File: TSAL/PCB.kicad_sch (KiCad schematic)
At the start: 62 parts, among them J1 TE 770966-2, J2 JST B04B-XASK, J3 Conn_01x02, J4 Conn_01x02, Q1 IRLZ44N, Q2 MMBT3904, Q3 IRLZ44N, U1 TL431D, U2 LMV331, U3 UCC12040DVE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

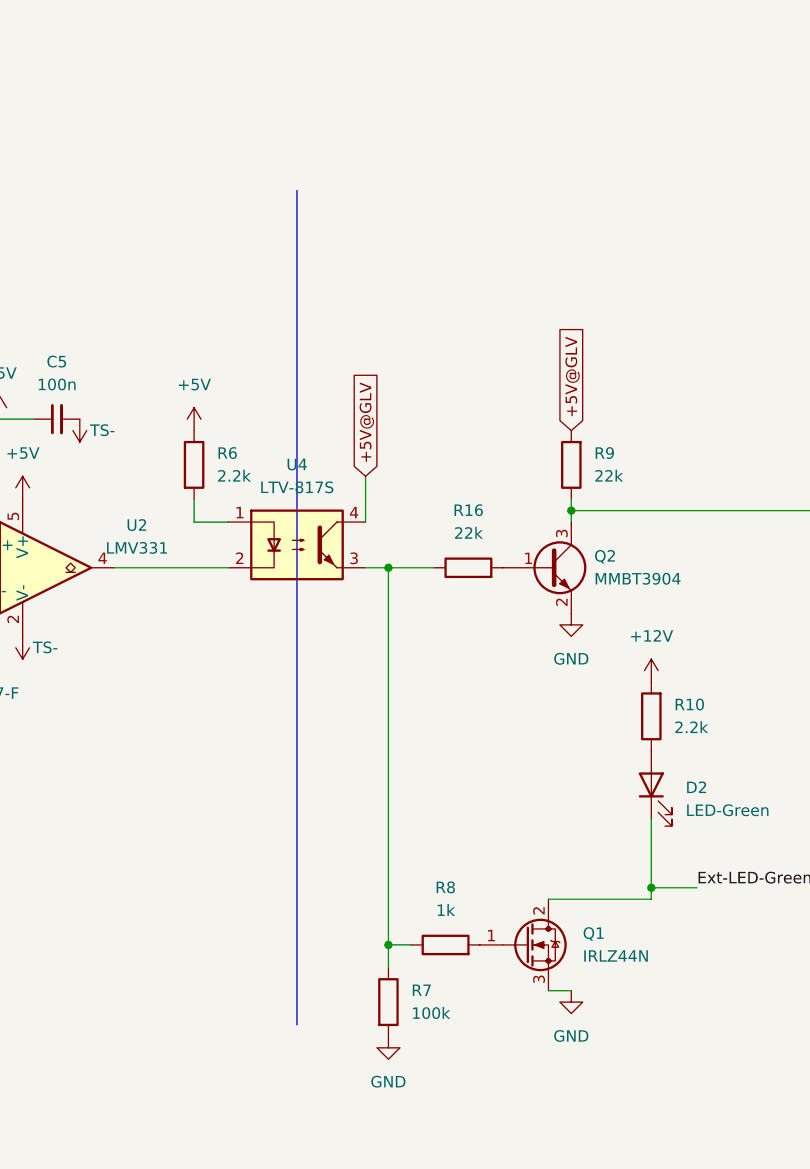
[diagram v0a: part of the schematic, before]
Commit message: fix low voltage circuit
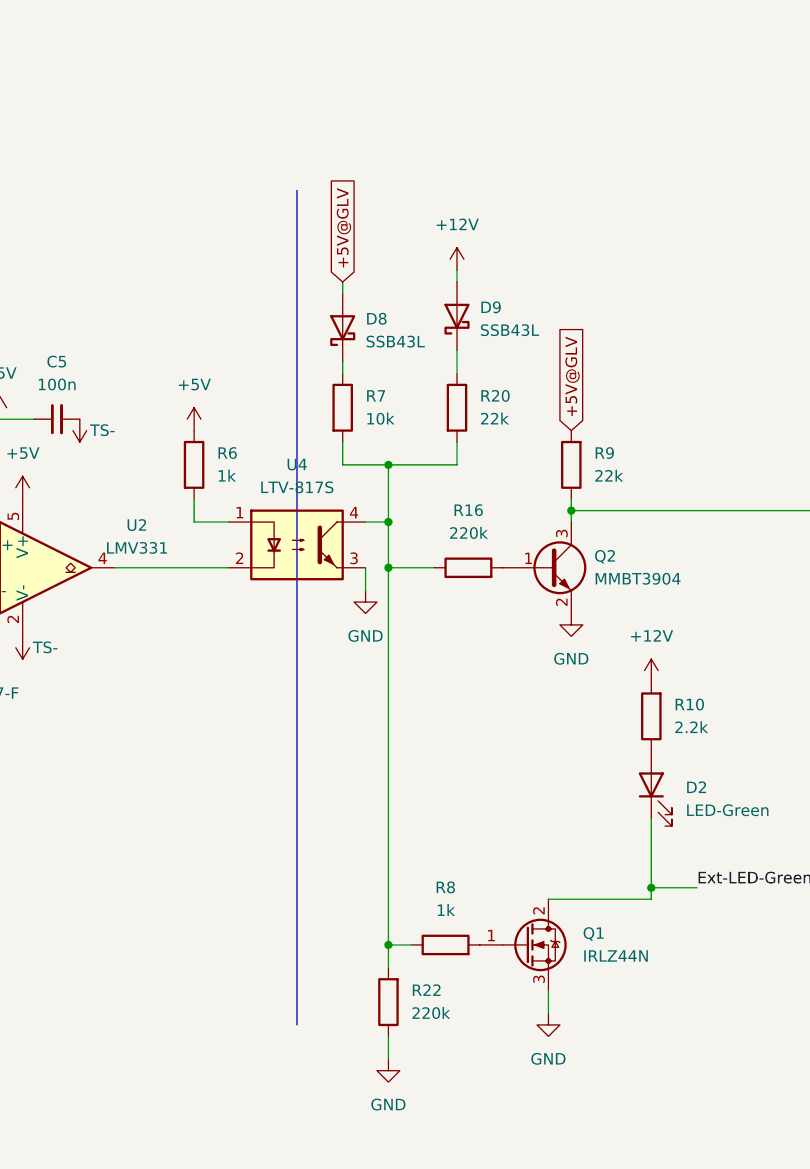
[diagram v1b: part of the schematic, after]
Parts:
- added D8, D9: SSB43L, Diode_SMD:D_SMB, symbol Device:D_Schottky
- added R20: 22k, Resistor_SMD:R_0603_1608Metric, symbol Device:R
- added R22: 220k, Resistor_SMD:R_0603_1608Metric, symbol Device:R
- R16: value 22k -> 220k
- R6: value 2.2k -> 1k
- R7: value 100k -> 10k
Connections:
- net +12V: now also D9.2 (A)
- net +5V@GLV: now also D8.2 (A); no longer U4.4
- net GND: now also U4.3, R22.1; no longer R7.2
- net at R16.1, R8.1: now also R7.2, U4.4, R20.2, R22.2; no longer R7.1, U4.3
- new net: D8.1 (K), R7.1
- new net: D9.1 (K), R20.1

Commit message: TSAL REV3 :(
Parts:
- removed D4: AES2JF-HF, KiCADv6:CR_SMAF_CIP, symbol Device:D_Schottky
- added C15: 100u, Capacitor_SMD:CP_Elec_6.3x7.7, symbol Device:C_Polarized_Small
- added C8: 470p, Capacitor_SMD:C_0603_1608Metric, symbol Device:C_Small
- added D10: 1N4148WS, Diode_SMD:D_SOD-123, symbol Device:D
- added D4: STTH1R06A, Diode_SMD:D_SMA, symbol Device:D
- added JP1: SolderJumper_2_Bridged, Jumper:SolderJumper-2_P1.3mm_Bridged_RoundedPad1.0x1.5mm, symbol Jumper:SolderJumper_2_Bridged
- added R23: 24k, Resistor_SMD:R_0603_1608Metric, symbol Device:R_Small
- added R24: 1k, Resistor_SMD:R_0603_1608Metric, symbol Device:R_Small
- added TP1, TP2, TP3, TP4, TP5, TP6: TestPoint, TestPoint:TestPoint_Keystone_5019_Minature, symbol Connector:TestPoint
- added U6: LF50_TO252, Package_TO_SOT_SMD:TO-252-2, symbol Regulator_Linear:LF50_TO252
- C1: value 100n -> 220n
- C2: value 100u -> 0.1u; now not fitted
- L1: footprint Inductor_SMD:L_1008_2520Metric -> Inductor_SMD:L_12x12mm_H8mm
- R17, R18: value 5k -> 20k
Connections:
- net +5V: now also JP1.2 (B), R24.1, U6.3 (VO); no longer C2.1, D6.2 (A), L1.2
- net TS-: now also C15.2, D4.2 (A), R24.2, TP6.1, U6.2 (GND)
- net at C1.1, D6.1 (K), R17.1: now also D10.2 (A)
- net at R17.2, R18.1, U7.2 (FB): now also C8.1, TP2.1
- net at RV1.2, U2.1 (+): now also TP5.1
- net at C1.2, C7.2, L1.1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: now also C8.2, D4.1 (K), TP3.1
- net at C7.1, U7.1 (VCC): now also R23.1, TP1.1
- new net: C15.1, C2.1, D6.2 (A), JP1.1 (A), L1.2, TP4.1, U6.1 (VI)
- new net: D10.1 (K), R23.2
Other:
- moved on the sheet: C1, C10, C11, C12, C13, C14, C3, C4, C5, C6, C7, C9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

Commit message: TSAL V3 Minor changes
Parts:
- H1, H2, H3, H4: footprint MountingHole:MountingHole_4mm -> MountingHole:MountingHole_3.2mm_M3
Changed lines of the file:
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@@
   (symbol (lib_id "Mechanical:MountingHole") (at 88.9 233.68 0) (unit 1)
     (in_bom yes) (on_board yes) (dnp no)
-    (property "Reference" "H3" (at 88.9 228.6 0)
-      (effects (font (size 1.27 1.27)))
-    )
-    (property "Value" "MountingHole" (at 88.9 230.505 0)
-      (effects (font (size 1.27 1.27)))
-    )
-    (property "Footprint" "MountingHole:MountingHole_4mm" (at 88.9 233.68 0)
+    (property "Reference" "H3" (at 92.71 232.41 0)
+      (effects (font (size 1.27 1.27)))
+    )
+    (property "Value" "MountingHole" (at 97.79 234.95 0)
+      (effects (font (size 1.27 1.27)))
+    )
+    (property "Footprint" "MountingHole:MountingHole_3.2mm_M3" (at 88.9 233.68 0)
       (effects (font (size 1.27 1.27)) hide)
     )
@@
       (effects (font (size 1.27 1.27)) (justify left))
     )
-    (property "Footprint" "MountingHole:MountingHole_4mm" (at 88.9 240.03 0)
+    (property "Footprint" "MountingHole:MountingHole_3.2mm_M3" (at 88.9 240.03 0)
       (effects (font (size 1.27 1.27)) hide)
     )
@@
   (symbol (lib_id "Mechanical:MountingHole") (at 88.9 224.79 0) (unit 1)
     (in_bom yes) (on_board yes) (dnp no)
-    (property "Reference" "H2" (at 88.9 219.71 0)
-      (effects (font (size 1.27 1.27)))
-    )
-    (property "Value" "MountingHole" (at 88.9 221.615 0)
-      (effects (font (size 1.27 1.27)))
-    )
-    (property "Footprint" "MountingHole:MountingHole_4mm" (at 88.9 224.79 0)
+    (property "Reference" "H2" (at 92.71 223.52 0)
+      (effects (font (size 1.27 1.27)))
+    )
+    (property "Value" "MountingHole" (at 97.79 226.06 0)
+      (effects (font (size 1.27 1.27)))
+    )
+    (property "Footprint" "MountingHole:MountingHole_3.2mm_M3" (at 88.9 224.79 0)
       (effects (font (size 1.27 1.27)) hide)
     )
@@
   (symbol (lib_id "Mechanical:MountingHole") (at 88.9 215.9 0) (unit 1)
     (in_bom yes) (on_board yes) (dnp no)
-    (property "Reference" "H1" (at 88.9 210.82 0)
-      (effects (font (size 1.27 1.27)))
-    )
-    (property "Value" "MountingHole" (at 88.9 212.725 0)
-      (effects (font (size 1.27 1.27)))
-    )
-    (property "Footprint" "MountingHole:MountingHole_4mm" (at 88.9 215.9 0)
-      (effects (font (size 1.27 1.27)) hide)
-    )
+    (property "Reference" "H1" (at 92.71 214.63 0)
+      (effects (font (size 1.27 1.27)))
+    )
+    (property "Value" "MountingHole" (at 97.79 217.17 0)
+      (effects (font (size 1.27 1.27)))
+    )
+    (property "Footprint" "MountingHole:MountingHole_3.2mm_M3" (at 88.9 215.9 0)
+      (effects (font (size 1.27 1.27)) hide)
+    )

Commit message: Minor changes once again
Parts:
- C3, C5, C6: value 100n -> 0.1u
- L2: footprint Inductor_SMD:L_1008_2520Metric -> Inductor_SMD:L_1210_3225Metric
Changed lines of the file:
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@@
       (effects (font (size 1.27 1.27)))
     )
-    (property "Value" "100n" (at 242.5763 146.05 90)
+    (property "Value" "0.1u" (at 242.5763 146.05 90)
       (effects (font (size 1.27 1.27)))
     )
@@
       (effects (font (size 1.27 1.27)))
     )
-    (property "Value" "100n" (at 234.95 161.29 90)
+    (property "Value" "0.1u" (at 234.95 161.29 90)
       (effects (font (size 1.27 1.27)))
     )
@@
       (effects (font (size 1.27 1.27)))
     )
-    (property "Value" "100n" (at 144.7863 157.48 90)
+    (property "Value" "0.1u" (at 144.7863 157.48 90)
       (effects (font (size 1.27 1.27)))
     )
@@
       (effects (font (size 1.27 1.27)))
     )
-    (property "Footprint" "Inductor_SMD:L_1008_2520Metric" (at 67.31 52.07 0)
-      (effects (font (size 1.27 1.27)) hide)
-    )
+    (property "Footprint" "Inductor_SMD:L_1210_3225Metric" (at 67.31 52.07 0)
+      (effects (font (size 1.27 1.27)) hide)
+    )

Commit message: Footprint change
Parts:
- D10: footprint Diode_SMD:D_SOD-123 -> Diode_SMD:D_SOD-323
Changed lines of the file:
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@@
       (effects (font (size 1.27 1.27)))
     )
-    (property "Footprint" "Diode_SMD:D_SOD-123" (at 151.13 46.99 0)
+    (property "Footprint" "Diode_SMD:D_SOD-323" (at 151.13 46.99 0)
       (effects (font (size 1.27 1.27)) hide)
     )

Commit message: JP1 Edit
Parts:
- removed JP1: SolderJumper_2_Bridged, Jumper:SolderJumper-2_P1.3mm_Bridged_RoundedPad1.0x1.5mm, symbol Jumper:SolderJumper_2_Bridged
- added JP1: SolderJumper_2_Open, Jumper:SolderJumper-2_P1.3mm_Open_RoundedPad1.0x1.5mm, symbol Jumper:SolderJumper_2_Open
- C2: now fitted
- U6: value LF50_TO252 -> L7805; symbol Regulator_Linear:LF50_TO252 -> Regulator_Linear:L7805; now fitted
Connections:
- net +5V: now also JP1.2 (B)
- net at C15.1, C2.1, D6.2 (A)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: now also JP1.1 (A)
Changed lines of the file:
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@@
     )
   )
-  (symbol (lib_id "Regulator_Linear:LF50_TO252") (at 200.66 58.42 0) (unit 1)
-    (in_bom yes) (on_board yes) (dnp yes) (fields_autoplaced)
+  (symbol (lib_id "Regulator_Linear:L7805") (at 200.66 58.42 0) (unit 1)
+    (in_bom yes) (on_board yes) (dnp no) (fields_autoplaced)
     (property "Reference" "U6" (at 200.66 52.07 0)
       (effects (font (size 1.27 1.27)))
     )
-    (property "Value" "LF50_TO252" (at 200.66 54.61 0)
-      (effects (font (size 1.27 1.27)))
-    )
-    (property "Footprint" "Package_TO_SOT_SMD:TO-252-2" (at 200.66 52.705 0)
-      (effects (font (size 1.27 1.27) italic) hide)
-    )
-    (property "Datasheet" "http://www.st.com/content/ccc/resource/technical/document/datasheet/c4/0e/7e/2a/be/bc/4c/bd/CD00000546.pdf/files/CD00000546.pdf/jcr:content/translations/en.CD00000546.pdf" (at 200.66 59.69 0)
+    (property "Value" "L7805" (at 200.66 54.61 0)
+      (effects (font (size 1.27 1.27)))
+    )
+    (property "Footprint" "Package_TO_SOT_SMD:TO-252-2" (at 201.295 62.23 0)
+      (effects (font (size 1.27 1.27) italic) (justify left) hide)
+    )
+    (property "Datasheet" "http://www.st.com/content/ccc/resource/technical/document/datasheet/41/4f/b3/b0/12/d4/47/88/CD00000444.pdf/files/CD00000444.pdf/jcr:content/translations/en.CD00000444.pdf" (at 200.66 59.69 0)
       (effects (font (size 1.27 1.27)) hide)
     )
@@
     )
   )
+  (symbol (lib_id "Jumper:SolderJumper_2_Open") (at 200.66 48.26 0) (unit 1)
+    (in_bom yes) (on_board yes) (dnp no)
+    (property "Reference" "JP1" (at 200.66 41.91 0)
+      (effects (font (size 1.27 1.27)))
+    )
+    (property "Value" "SolderJumper_2_Open" (at 205.74 44.45 0)
+      (effects (font (size 1.27 1.27)))
+    )
+    (property "Footprint" "Jumper:SolderJumper-2_P1.3mm_Open_RoundedPad1.0x1.5mm" (at 200.66 48.26 0)
+      (effects (font (size 1.27 1.27)) hide)
+    )
+    (property "Datasheet" "~" (at 200.66 48.26 0)
+      (effects (font (size 1.27 1.27)) hide)
+    )
+    (pin "1")
+    (pin "2")
+    (instances
+      (project "PCB"
+        (path "/68f34db6-b185-48e2-8817-fb07f7d1240e"
+          (reference "JP1") (unit 1)
+        )
+      )
+    )
+  )
   (symbol (lib_id "Device:C_Small") (at 312.42 52.07 0) (unit 1)
     (in_bom yes) (on_board yes) (dnp no) (fields_autoplaced)
@@
   )
   (symbol (lib_id "Device:C_Small") (at 189.23 63.5 0) (unit 1)
-    (in_bom yes) (on_board yes) (dnp yes) (fields_autoplaced)
+    (in_bom yes) (on_board yes) (dnp no) (fields_autoplaced)
     (property "Reference" "C2" (at 191.77 62.2363 0)
       (effects (font (size 1.27 1.27)) (justify left))
@@
         )
       )
-    )
-  )
-  (symbol (lib_id "Jumper:SolderJumper_2_Bridged") (at 200.66 48.26 0) (unit 1)
-    (in_bom yes) (on_board yes) (dnp no)
-    (property "Reference" "JP1" (at 200.66 45.72 0)
-      (effects (font (size 1.27 1.27)))
-    )
-    (property "Value" "SolderJumper_2_Bridged" (at 200.66 44.45 0)
-      (effects (font (size 1.27 1.27)) hide)
-    )
-    (property "Footprint" "Jumper:SolderJumper-2_P1.3mm_Bridged_RoundedPad1.0x1.5mm" (at 200.66 48.26 0)
-      (effects (font (size 1.27 1.27)) hide)
-    )
-    (property "Datasheet" "~" (at 200.66 48.26 0)
-      (effects (font (size 1.27 1.27)) hide)
-    )
-    (pin "1")
-    (pin "2")
-    (instances
-      (project "PCB"
-        (path "/68f34db6-b185-48e2-8817-fb07f7d1240e"
-          (reference "JP1") (unit 1)
-        )
-      )
